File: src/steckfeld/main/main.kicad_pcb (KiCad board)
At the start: 2 copper layers, 127.5 x 53.3 mm, 46 parts, among them J1 IDC Header, J10 IN, J11 Conn_01x04_Female, J2 IN, J3 IN, J4 IN, J5 IN, J6 Conn_01x02_Female, J7 Conn_01x04_Female, J8 Conn_01x04_Female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

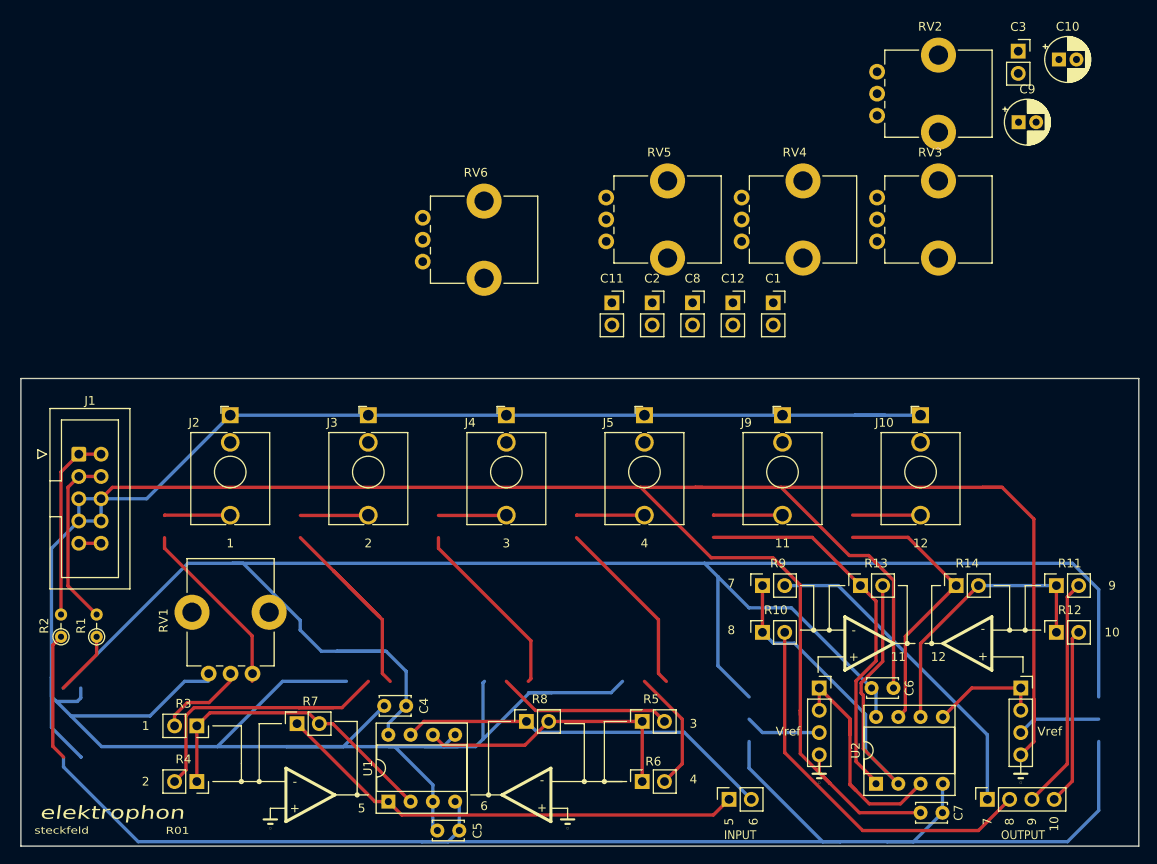
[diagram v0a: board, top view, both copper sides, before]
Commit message: update to latest elektron version
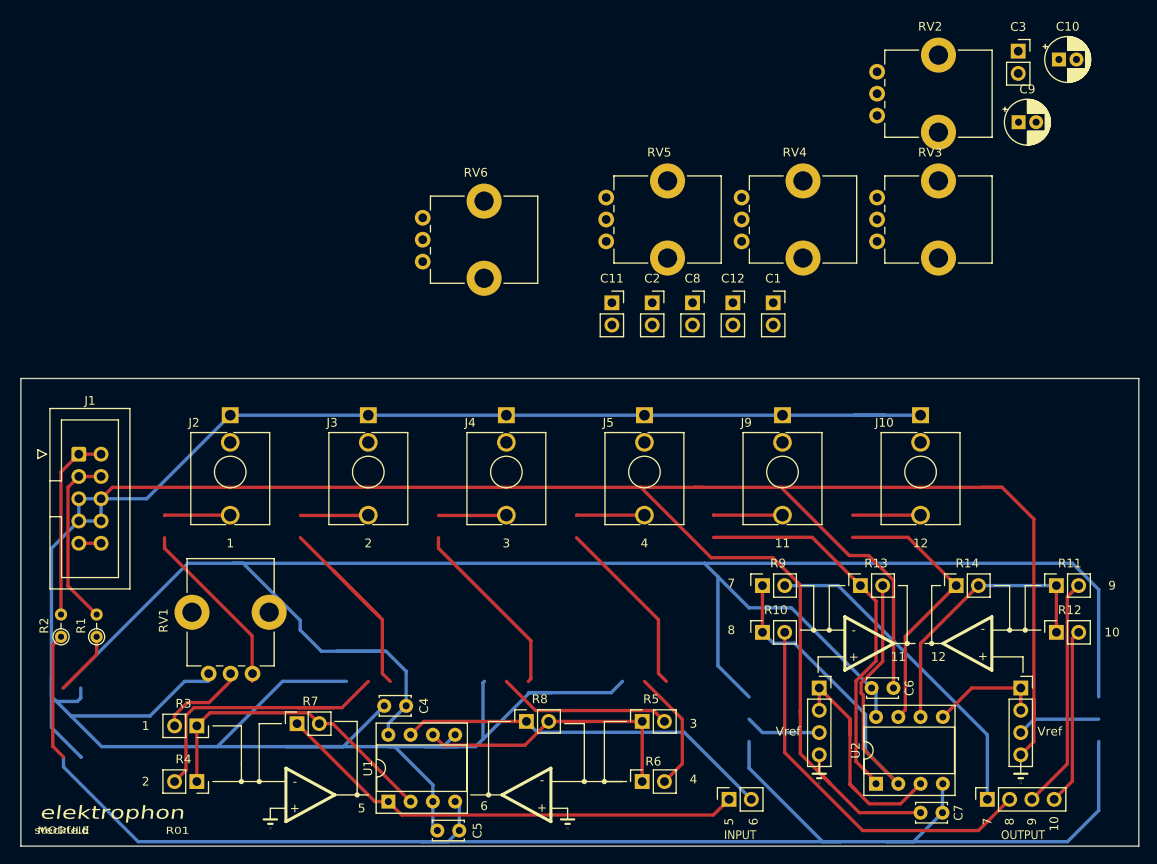
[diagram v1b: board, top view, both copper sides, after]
